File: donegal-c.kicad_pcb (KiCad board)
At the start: 2 copper layers, 285.8 x 123.8 mm, 155 parts, among them J2 ISP, SW1 SW_SPST, SW10 SW_SPST, SW11 SW_SPST, SW12 SW_SPST, SW13 SW_SPST, SW14 SW_SPST, SW16 SW_SPST, SW17 SW_SPST, SW18 SW_SPST, SW19 SW_SPST, SW2 SW_SPST, SW20 SW_SPST, SW21 SW_SPST, SW22 SW_SPST, SW23 SW_SPST, SW24 SW_SPST, SW25 SW_SPST, SW26 SW_SPST, SW27 SW_SPST, SW28 SW_SPST, SW3 SW_SPST, SW30 SW_SPST, SW31 SW_SPST, SW32 SW_SPST, SW33 SW_SPST, SW34 SW_SPST, SW35 SW_SPST, SW36 SW_SPST, SW37 SW_SPST, SW38 SW_SPST, SW39 SW_SPST, SW4 SW_SPST, SW40 SW_SPST, SW41 SW_SPST, SW42 SW_SPST, SW45 SW_SPST, SW46 SW_SPST, SW48 SW_SPST, SW49 SW_SPST, SW5 SW_SPST, SW50 SW_SPST, SW51 SW_SPST, SW52 SW_SPST, SW53 SW_SPST, SW54 SW_SPST, SW55 SW_SPST, SW56 SW_SPST, SW57 SW_SPST, SW6 SW_SPST, SW60 SW_SPST, SW61 SW_SPST, SW62 SW_SPST, SW64 SW_SPST, SW65 SW_SPST, SW66 SW_SPST, SW67 SW_SPST, SW68 RESET, SW69 BOOT, SW7 SW_SPST, SW76 SW_SPST, SW8 SW_SPST, SW80 SW_SPST, SW82 SW_SPST, SW9 SW_SPST, U1 ATmega328-PU, Y1 16MHZ

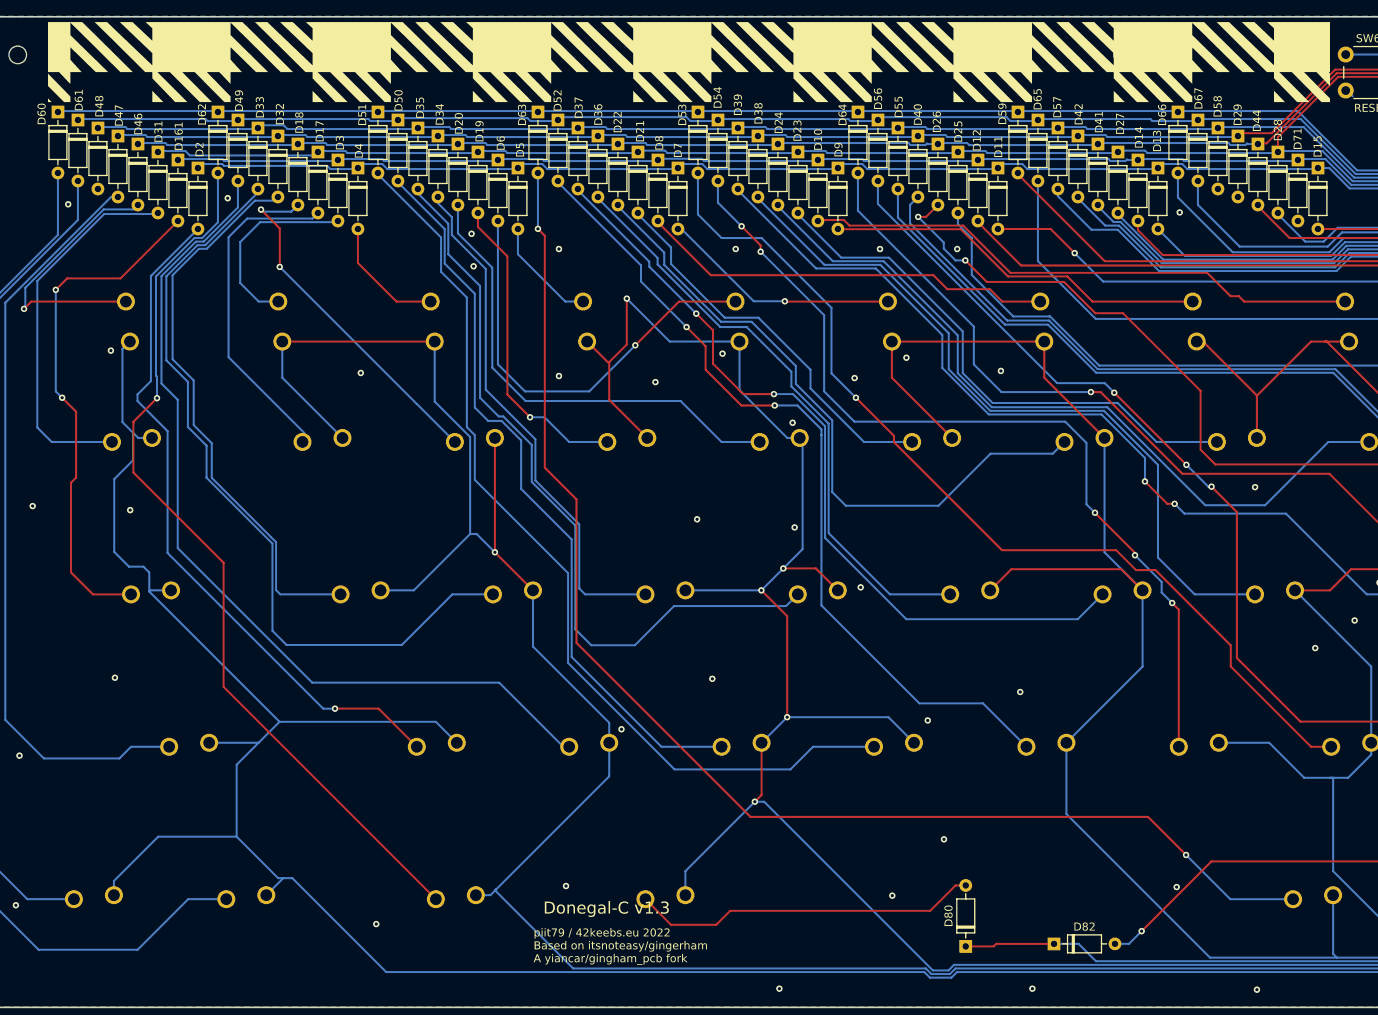
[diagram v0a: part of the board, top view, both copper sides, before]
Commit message: removed pattern and text from silkscreen
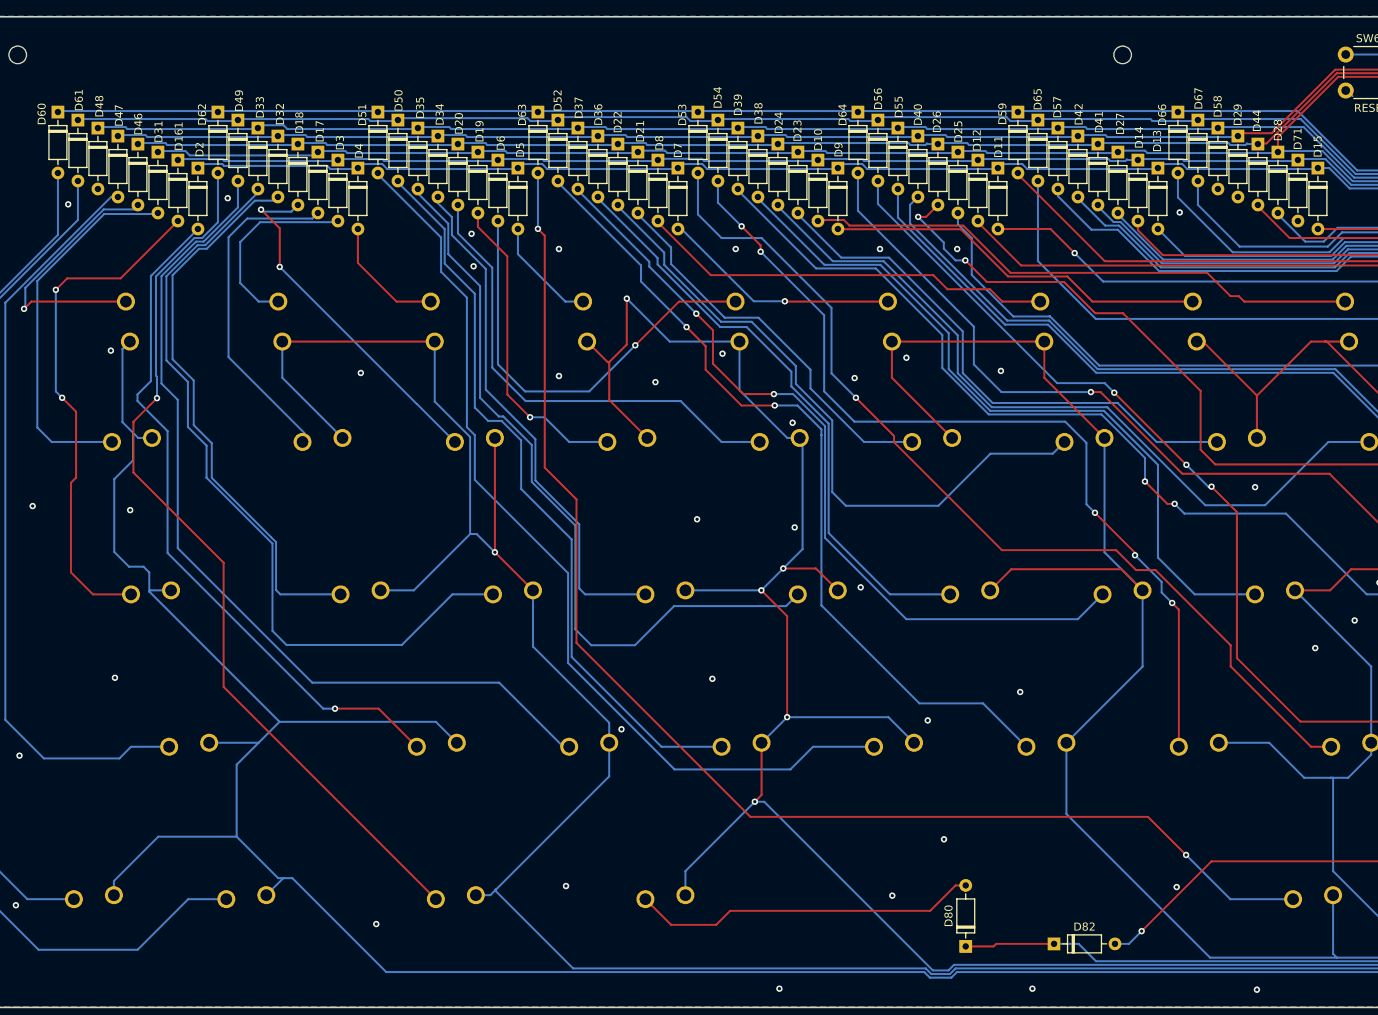
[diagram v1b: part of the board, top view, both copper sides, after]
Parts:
- removed PATTERN1: Gingham, tartan:gingham
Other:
- board text removed: "Donegal-C v1.3"
- board text removed: "piit79 / 42keebs.eu 2022 Based on itsnoteasy/gingerham A yiancar/gingham_pcb fork"

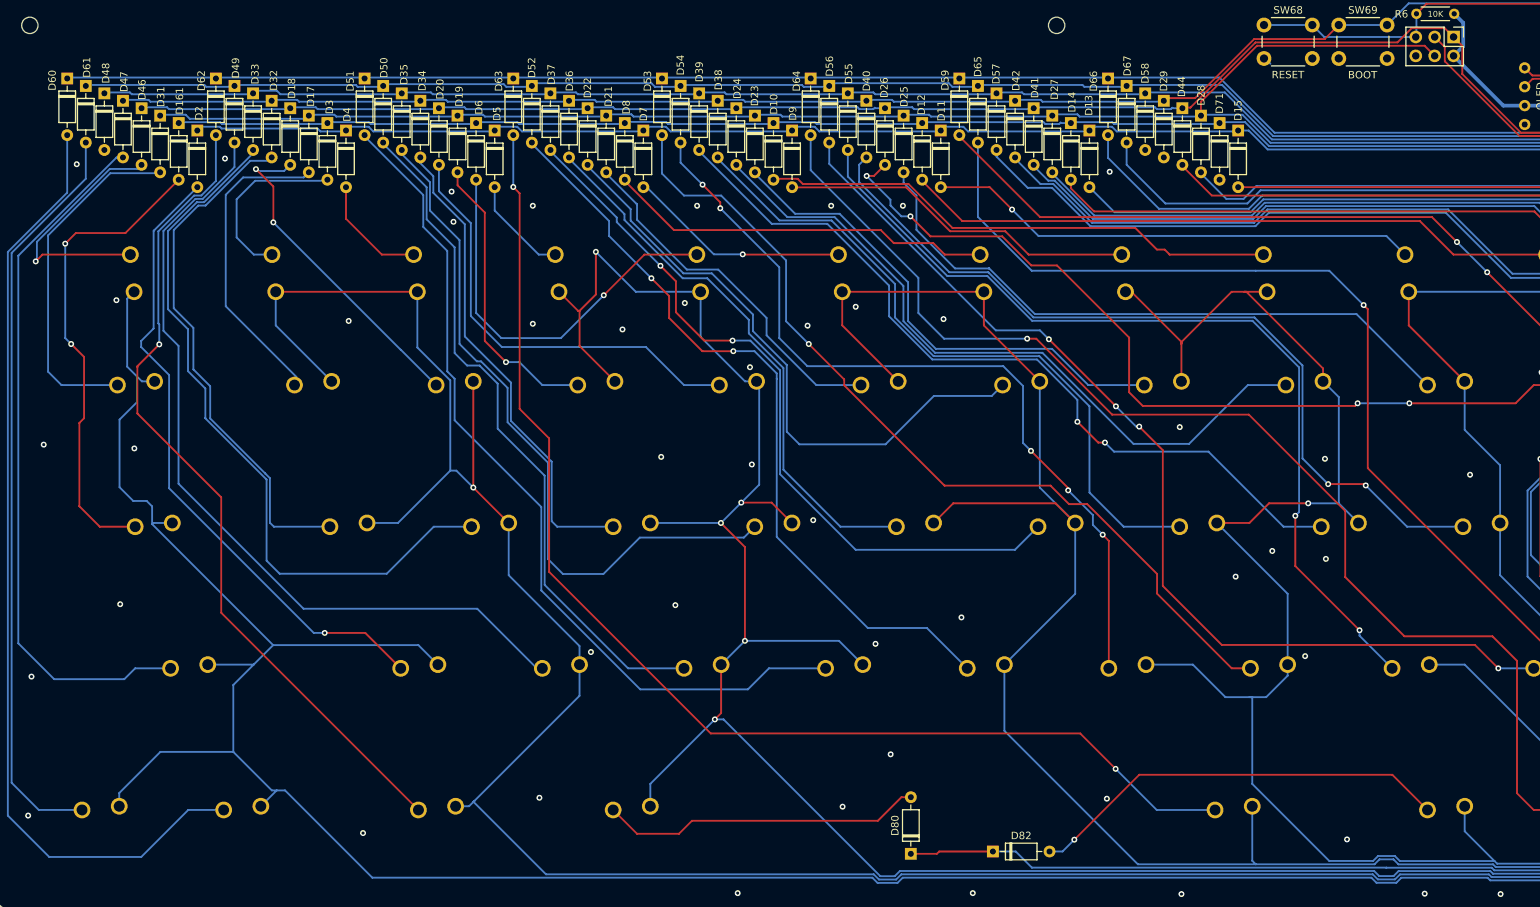
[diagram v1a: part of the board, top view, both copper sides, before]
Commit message: changed spacebar to wider hole and moved some silk
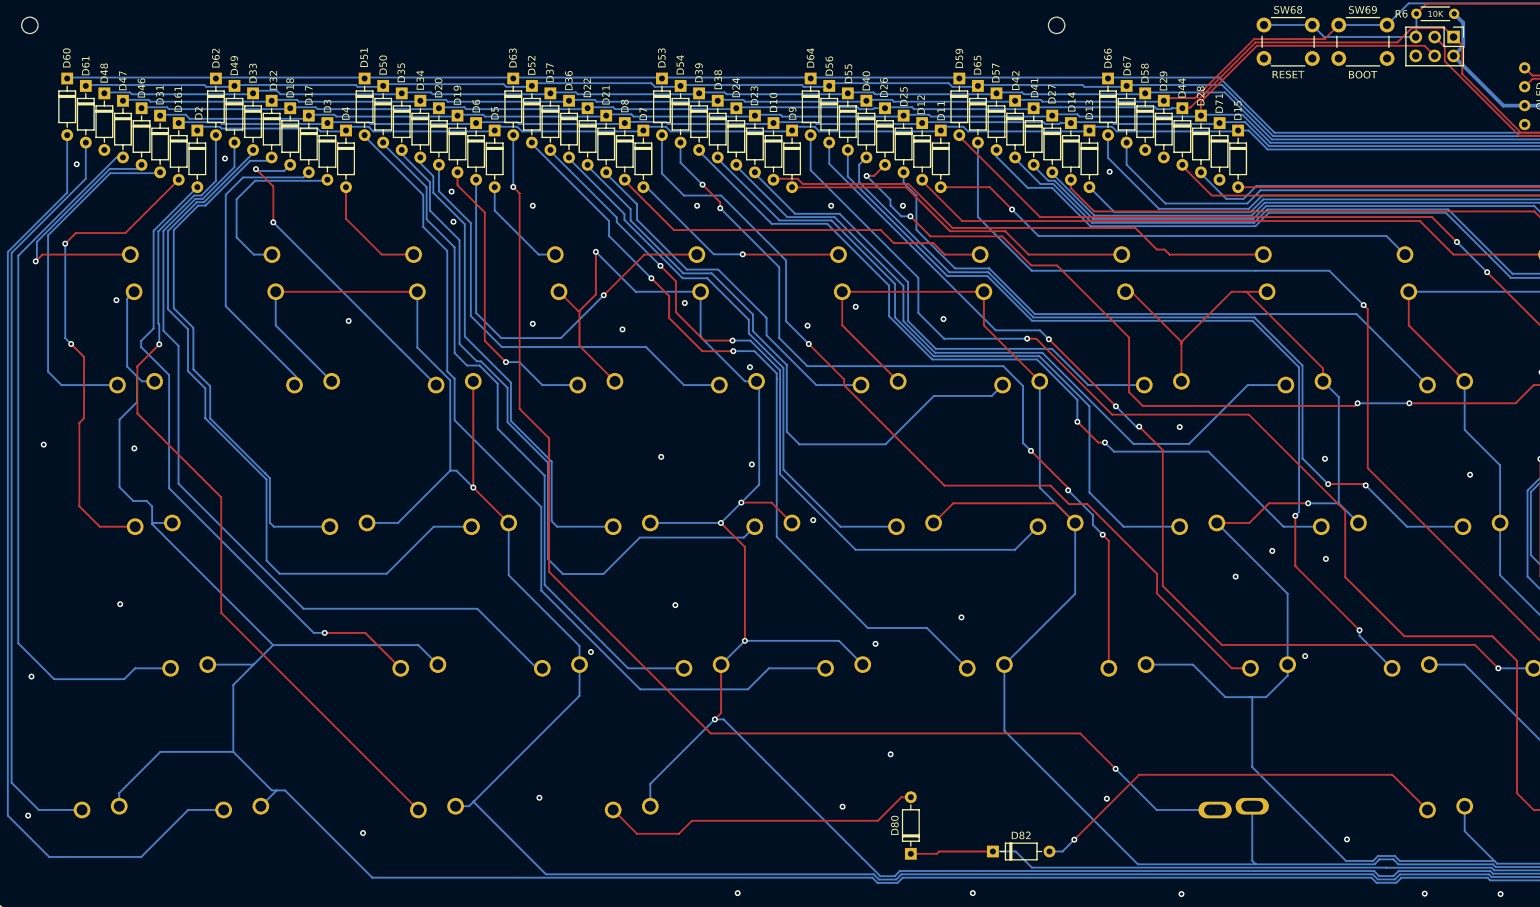
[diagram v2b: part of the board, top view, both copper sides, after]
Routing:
- net col4: track 380.3 -> 379.0 mm

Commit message: added JLCJLCJLCJLC to place order number under MCU
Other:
- board text added: "JLCJLCJLCJLC"
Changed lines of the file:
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@@
   (gr_line (start 70.04875 89.844) (end 351.03625 89.844) (layer "Edge.Cuts") (width 0.2))
   (gr_arc (start 67.6675 92.22525) (mid 68.364952 90.541452) (end 70.04875 89.844) (layer "Edge.Cuts") (width 0.2))
+  (gr_text "JLCJLCJLCJLC" (at 330.718 103.876) (layer "F.SilkS")
+    (effects (font (size 1 1) (thickness 0.15)))
+  )
   (segment (start 286.849 98.33813) (end 287.694 97.49313) (width 0.25) (layer "F.Cu") (net 1))
   (segment (start 287.429761 99.4445) (end 287.4445 99.4445) (width 0.25) (layer "B.Cu") (net 1))

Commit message: rework by jakob
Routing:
- net Net-(D22-Pad2): track 82.1 -> 70.4 mm
- net col6: track 292.6 -> 281.4 mm
- net col5: track 319.4 -> 309.4 mm
- net col4: track 379.0 -> 370.1 mm
- net Net-(D35-Pad2): track 94.2 -> 86.4 mm
- net Net-(D3-Pad2): track 23.9 -> 16.2 mm
- net Net-(D18-Pad2): track 44.2 -> 37.8 mm, vias 2 -> 1
- net Net-(D17-Pad2): track 40.9 -> 35.3 mm
- net Net-(D57-Pad2): track 154.4 -> 159.6 mm
- net Net-(D49-Pad2): track 109.7 -> 104.7 mm
- net Net-(D42-Pad2): track 157.3 -> 162.2 mm
- net Net-(D33-Pad2): track 96.5 -> 92.6 mm
- net Net-(D46-Pad2): track 34.2 -> 30.3 mm
- net col0: track 503.4 -> 500.1 mm
- net Net-(D26-Pad2): track 116.3 -> 113.0 mm, vias 4 -> 3
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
